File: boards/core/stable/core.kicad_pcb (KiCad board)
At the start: 2 copper layers, 215 x 100 mm, 361 parts, among them J201 Conn_02x08_Counter_Clockwise, J202 Conn_02x08_Counter_Clockwise, J203 Conn_02x08_Counter_Clockwise, J204 Conn_02x08_Counter_Clockwise, J214 Conn_02x04_Counter_Clockwise, Q201 2N3906, Q202 BC847BS, Q203 MMBFJ111, Q204 2N3906, Q205 BC847BS, Q206 MMBFJ111, Q207 BC847BS, Q208 BC548C, Q209 BC548C, Q210 BC548C, Q211 J111, Q212 MMBT5551, Q213 MMBT5551, Q214 MMBT5551, Q215 J111, U201 TL072, U202 TL072, U203 LM311, U204 TL072, U205 TL072, U206 LM311, U207 TL072, U208 TL072, U209 TL072, U210 TL072, U211 TL072, U212 4002, U213 LM358, U214 TL072, U215 CD4053B, U216 NE5532, U217 TL072, U218 TL072, U219 TL072, U220 TL072, U221 TL072, U222 TL072, U223 TL072, U225 TL072, U226 TL072, U227 TL072, U228 CD4040BM96

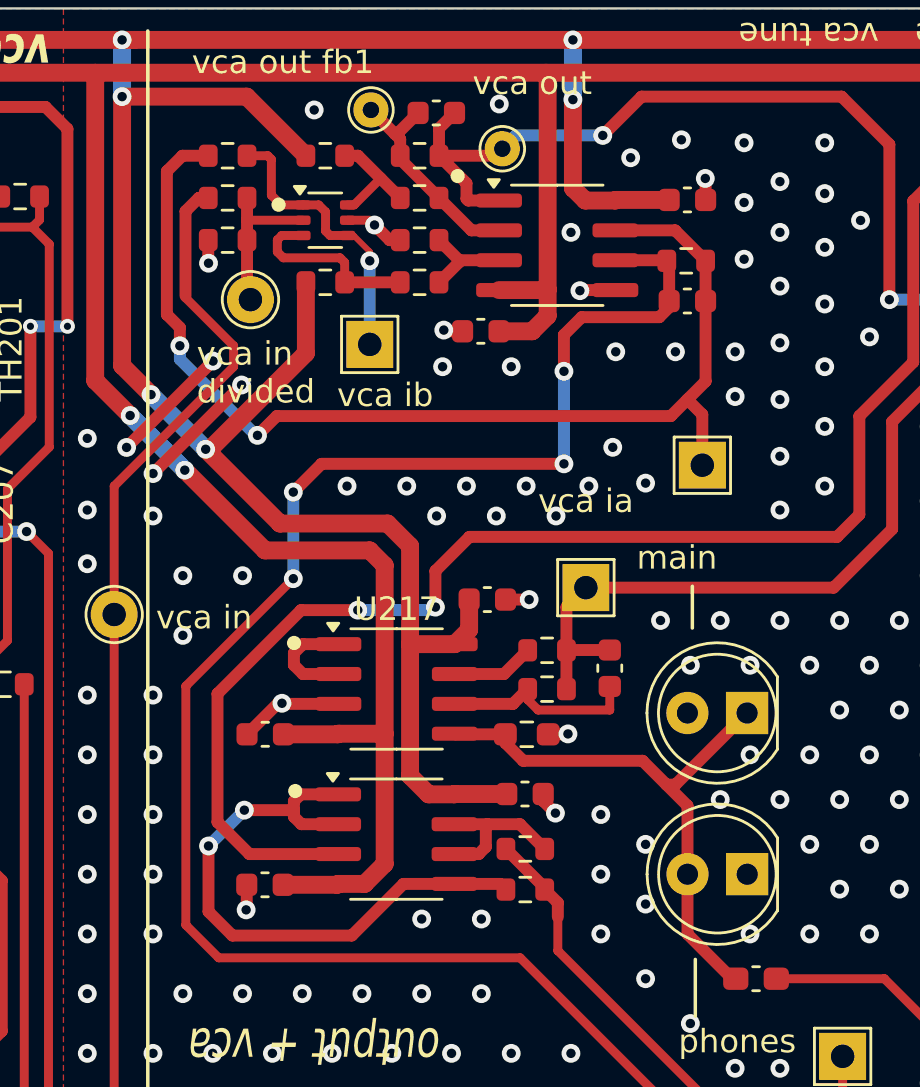
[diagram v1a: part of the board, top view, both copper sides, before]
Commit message: Replaced VCA dual BJT footprint
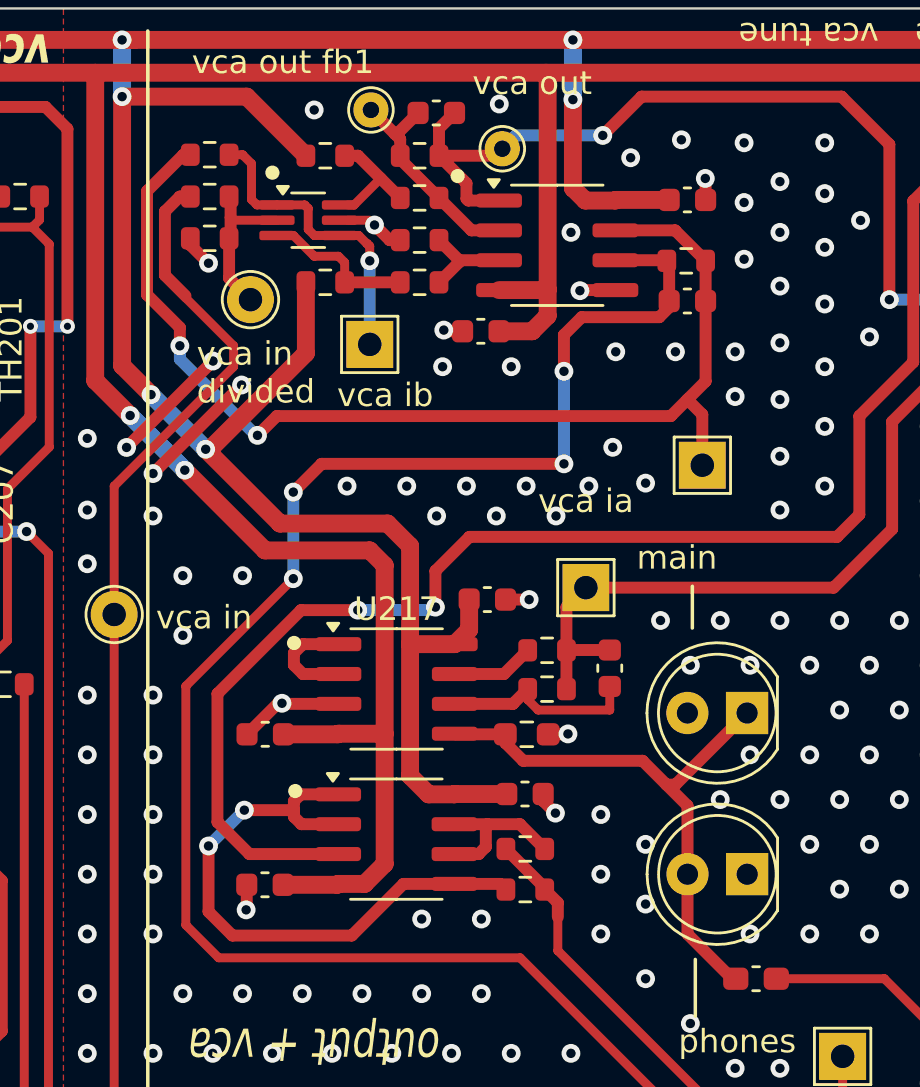
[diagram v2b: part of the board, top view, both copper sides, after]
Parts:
- Q207: footprint Package_TO_SOT_SMD:SOT-363_SC-70-6 -> Package_TO_SOT_SMD:SOT-363_SC-70-6_Handsoldering
- moved R233 0.77 mm to (162.2, 172.8)
- moved R232 0.76 mm to (162.2, 171.0)
- moved R236 0.76 mm to (162.2, 169.2)
- moved Q207 0.72 mm to (166.4, 172.0)
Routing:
- net Net-(Q207-C2): track 8.15 -> 6.78 mm
- net Net-(Q207-E1): track 12.2 -> 13.2 mm
